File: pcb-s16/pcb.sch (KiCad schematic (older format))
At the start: 12 parts, among them J1 USB_B_Micro, SW1 BTN, U1 PFS154-S16, U2 74HC595, U3 SLR0394DRC5BD, Y1 32.768kHz

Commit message: Update schematic
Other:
- moved on the sheet: C1, C2, J1, RN1, RN2, SW1, U2, U3

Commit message: Update schematic
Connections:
- net R3 renamed e
- net R4 renamed f
- net R7 renamed g
- net R8 renamed dp
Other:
- moved on the sheet: J1, RN2
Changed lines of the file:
@@
 Text Label 5850 2700 2    50   ~ 0
 PB3
-Text Label 5750 3250 2    50   ~ 0
+Text Label 5800 3100 2    50   ~ 0
 PB4
-Text Label 5750 3350 2    50   ~ 0
+Text Label 5800 3200 2    50   ~ 0
 PB5
-Text Label 6150 3050 0    50   ~ 0
+Text Label 6200 2900 0    50   ~ 0
 PB7
 Text Label 4350 2400 2    50   ~ 0
@@
 L Device:R_Pack04 RN2
 U 1 1 5F13C2E7
-P 5950 3250
-F 0 "RN2" V 6150 3250 50  0000 C CNN
-F 1 "R_Pack04" V 5624 3250 50  0001 C CNN
-F 2 "Resistor_SMD:R_Array_Convex_4x0603" V 6225 3250 50  0001 C CNN
-F 3 "~" H 5950 3250 50  0001 C CNN
-	1    5950 3250
+P 6000 3100
+F 0 "RN2" V 6200 3100 50  0000 C CNN
+F 1 "R_Pack04" V 5674 3100 50  0001 C CNN
+F 2 "Resistor_SMD:R_Array_Convex_4x0603" V 6275 3100 50  0001 C CNN
+F 3 "~" H 6000 3100 50  0001 C CNN
+	1    6000 3100
 	0    -1   1    0
 $EndComp
@@
 L Connector:USB_B_Micro J1
 U 1 1 5F1603EF
-P 3400 4400
-F 0 "J1" H 3457 4867 50  0000 C CNN
-F 1 "USB_B_Micro" H 3457 4776 50  0000 C CNN
-F 2 "modules:USB_Micro_B_Male" H 3550 4350 50  0001 C CNN
-F 3 "~" H 3550 4350 50  0001 C CNN
-	1    3400 4400
-	1    0    0    -1
-$EndComp
-Wire Wire Line
-	3300 4800 3400 4800
-Wire Wire Line
-	3700 4600 3700 4800
-Wire Wire Line
-	3700 4800 3400 4800
-Connection ~ 3400 4800
+P 3450 4300
+F 0 "J1" H 3507 4767 50  0000 C CNN
+F 1 "USB_B_Micro" H 3507 4676 50  0000 C CNN
+F 2 "modules:USB_Micro_B_Male" H 3600 4250 50  0001 C CNN
+F 3 "~" H 3600 4250 50  0001 C CNN
+	1    3450 4300
+	1    0    0    -1
+$EndComp
+Wire Wire Line
+	3350 4700 3450 4700
+Wire Wire Line
+	3750 4500 3750 4700
+Wire Wire Line
+	3750 4700 3450 4700
+Connection ~ 3450 4700
 $Comp
 L power:GND #PWR0109
 U 1 1 5F162B7F
-P 3400 4800
-F 0 "#PWR0109" H 3400 4550 50  0001 C CNN
-F 1 "GND" V 3405 4672 50  0000 R CNN
-F 2 "" H 3400 4800 50  0001 C CNN
-F 3 "" H 3400 4800 50  0001 C CNN
-	1    3400 4800
-	1    0    0    -1
-$EndComp
-NoConn ~ 3700 4400
-NoConn ~ 3700 4500
+P 3450 4700
+F 0 "#PWR0109" H 3450 4450 50  0001 C CNN
+F 1 "GND" V 3455 4572 50  0000 R CNN
+F 2 "" H 3450 4700 50  0001 C CNN
+F 3 "" H 3450 4700 50  0001 C CNN
+	1    3450 4700
+	1    0    0    -1
+$EndComp
+NoConn ~ 3750 4300
+NoConn ~ 3750 4400
 $Comp
 L power:VDD #PWR0110
 U 1 1 5F163A89
-P 3700 4200
-F 0 "#PWR0110" H 3700 4050 50  0001 C CNN
-F 1 "VDD" V 3717 4328 50  0000 L CNN
-F 2 "" H 3700 4200 50  0001 C CNN
-F 3 "" H 3700 4200 50  0001 C CNN
-	1    3700 4200
+P 3750 4100
+F 0 "#PWR0110" H 3750 3950 50  0001 C CNN
+F 1 "VDD" V 3767 4228 50  0000 L CNN
+F 2 "" H 3750 4100 50  0001 C CNN
+F 3 "" H 3750 4100 50  0001 C CNN
+	1    3750 4100
 	0    1    1    0
 $EndComp
@@
 Wire Wire Line
 	6500 2700 6250 2700
-Text Label 5750 3150 2    50   ~ 0
-R7
-Text Label 6150 3250 0    50   ~ 0
-R3
-Text Label 6150 3350 0    50   ~ 0
-R4
+Text Label 5800 3000 2    50   ~ 0
+g
+Text Label 6200 3100 0    50   ~ 0
+e
+Text Label 6200 3200 0    50   ~ 0
+f
 Text Label 6500 2800 2    50   ~ 0
-R3
+e
 Text Label 6500 2900 2    50   ~ 0
-R4
+f
 Text Label 6500 3000 2    50   ~ 0
-R7
+g
 Text Label 6500 3100 2    50   ~ 0
-R8
-Text Label 5750 3050 2    50   ~ 0
-R8
-Text Label 6150 3150 0    50   ~ 0
+dp
+Text Label 5800 2900 2    50   ~ 0
+dp
+Text Label 6200 3000 0    50   ~ 0
 PB6
 Wire Wire Line

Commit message: Update Crystal
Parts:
- Y1: footprint Crystal:Crystal_DS26_D2.0mm_L6.0mm_Horizontal -> Crystal:Crystal_C26-LF_D2.1mm_L6.5mm_Horizontal
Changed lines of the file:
@@
 EESchema Schematic File Version 4
-LIBS:pcb-cache
-EELAYER 26 0
+EELAYER 30 0
 EELAYER END
 $Descr A4 11693 8268
@@
 F 0 "Y1" V 3850 3000 50  0000 R CNN
 F 1 "32.768kHz" V 3850 2850 50  0000 R CNN
-F 2 "Crystal:Crystal_DS26_D2.0mm_L6.0mm_Horizontal" H 3850 2950 50  0001 C CNN
+F 2 "Crystal:Crystal_C26-LF_D2.1mm_L6.5mm_Horizontal" H 3850 2950 50  0001 C CNN
 F 3 "~" H 3850 2950 50  0001 C CNN
 	1    3850 2950

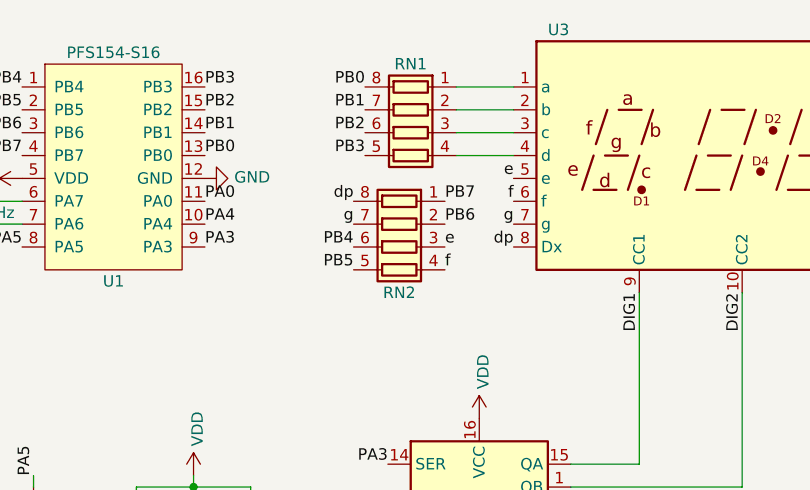
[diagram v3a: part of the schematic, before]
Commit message: Add values (680 ohm) for resistor arrays
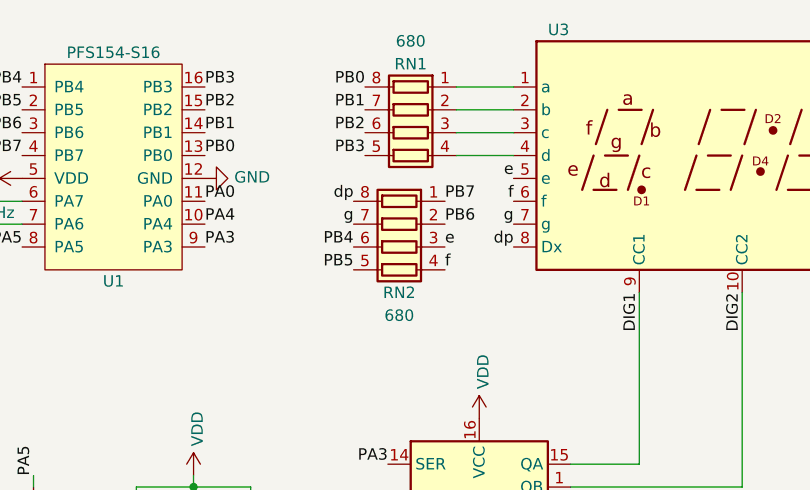
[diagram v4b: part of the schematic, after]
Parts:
- RN1, RN2: value R_Pack04 -> 680
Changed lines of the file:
@@
 P 6050 2600
 F 0 "RN1" V 5750 2600 50  0000 C CNN
-F 1 "R_Pack04" V 5724 2600 50  0001 C CNN
+F 1 "680" V 5650 2600 50  0000 C CNN
 F 2 "Resistor_SMD:R_Array_Convex_4x0603" V 6325 2600 50  0001 C CNN
 F 3 "~" H 6050 2600 50  0001 C CNN
@@
 P 6000 3100
 F 0 "RN2" V 6200 3100 50  0000 C CNN
-F 1 "R_Pack04" V 5674 3100 50  0001 C CNN
+F 1 "680" V 6300 3100 50  0000 C CNN
 F 2 "Resistor_SMD:R_Array_Convex_4x0603" V 6275 3100 50  0001 C CNN
 F 3 "~" H 6000 3100 50  0001 C CNN
